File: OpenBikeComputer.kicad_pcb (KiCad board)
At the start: 4 copper layers, 80 x 80 mm, 53 parts, among them J1 USB_C_Receptacle_USB2.0_14P, J2 RJ45_Shielded, J4 Micro_SD_Card_Det1, J5 Conn_01x24_Socket, J6 Conn_01x03_Pin, J7 RFShield_TwoPieces, J8 Conn_01x02_Socket, U1 nRF54L15-QFXX, U2 nPM1300-QEXX, U3 BQ298012RUGR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

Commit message: route SWD lines
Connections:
- J6 pad 1: Net-(J6-Pin_1) -> GND
- J6 pad 3: GND -> Net-(J6-Pin_3)
- U1 pad 25: Net-(J6-Pin_2) -> Net-(J6-Pin_3)
- U1 pad 26: Net-(J6-Pin_1) -> Net-(J6-Pin_2)
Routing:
- net Net-(J6-Pin_2): track 0.00 -> 49.3 mm, vias 0 -> 1
- net Net-(J6-Pin_3): track 0.00 -> 48.8 mm, vias 0 -> 1

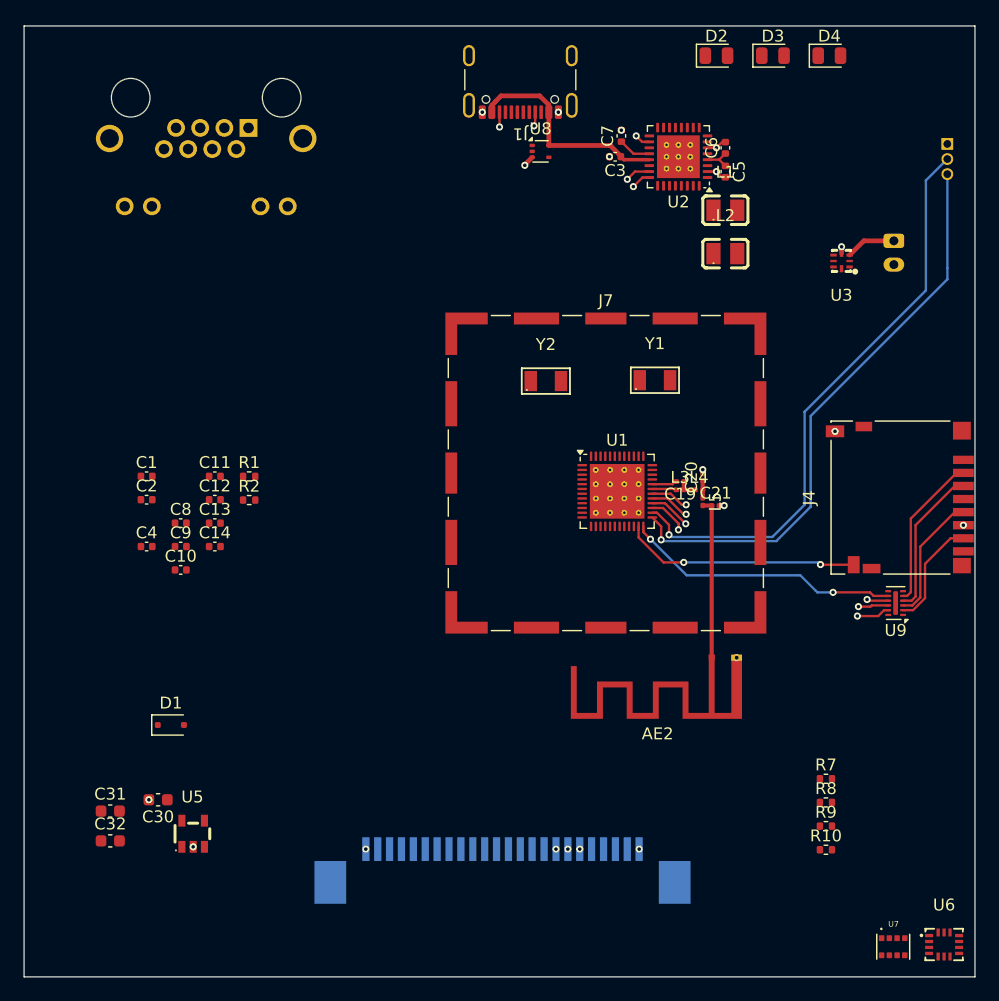
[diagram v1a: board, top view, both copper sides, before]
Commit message: add copper pour on all layers
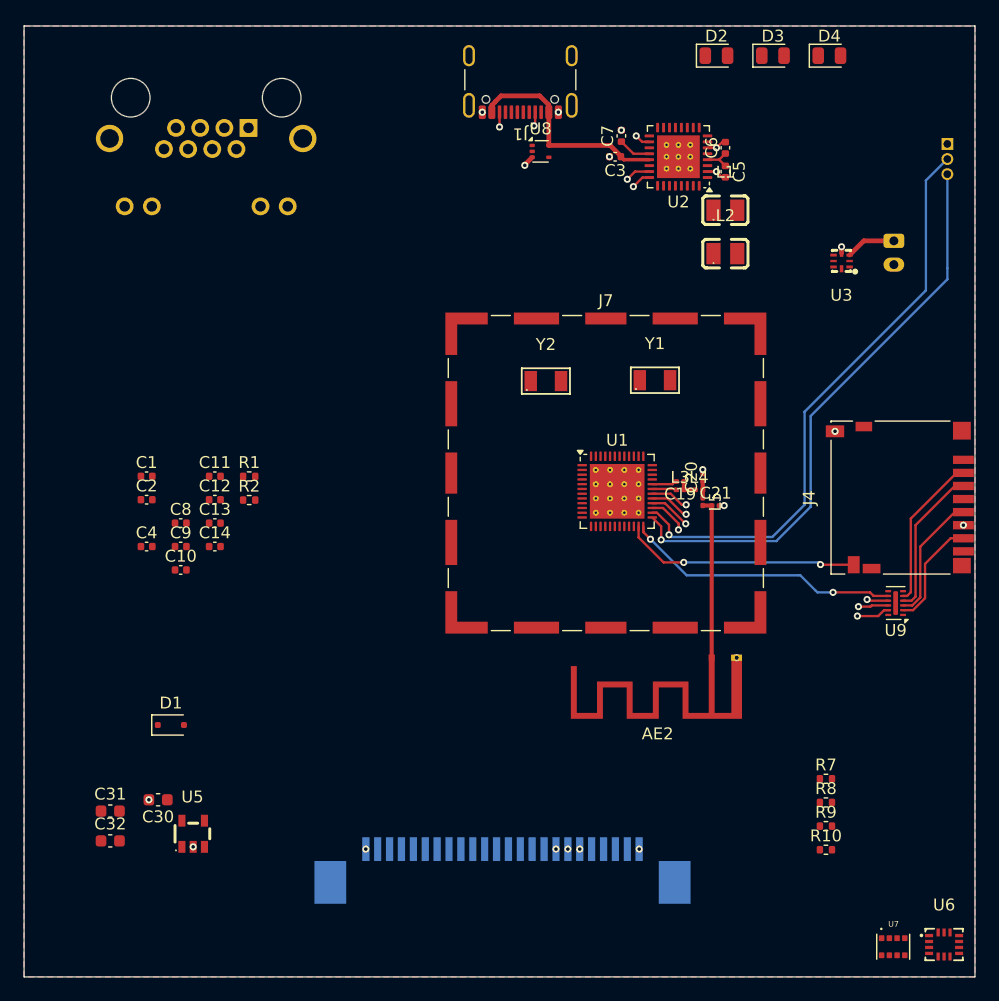
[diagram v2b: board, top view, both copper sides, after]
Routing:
- added copper zone on B.Cu, net GND
- added copper zone on F.Cu, net GND
- added copper zone on In2.Cu, net GND
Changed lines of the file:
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@@
 		(tags "capacitor")
 		(property "Reference" "C30"
-			(at 0 -1.43 360)
+			(at 0 -1.43 0)
 			(layer "F.SilkS")
 			(effects
@@
 		)
 		(property "Value" "4.7uF"
-			(at 0 1.43 360)
+			(at 0 1.43 0)
 			(layer "F.Fab")
 			(effects
@@
 		)
 		(fp_text user "${REFERENCE}"
-			(at 0 0 360)
+			(at 0 0 0)
 			(layer "F.Fab")
 			(effects
@@
 		(tags "capacitor")
 		(property "Reference" "C19"
-			(at 0 -1.05 360)
+			(at 0 -1.05 0)
 			(layer "F.SilkS")
 			(effects
@@
 		)
 		(property "Value" "1.5pF"
-			(at 0 1.05 360)
+			(at 0 1.05 0)
 			(layer "F.Fab")
 			(effects
@@
 		)
 		(fp_text user "${REFERENCE}"
-			(at 0 -0.68 360)
+			(at 0 -0.68 0)
 			(layer "F.Fab")
 			(effects
@@
 		(tags "X2QFN-8_L1.5-W1.5-P0.50-TL footprint C2873374")
 		(property "Reference" "U3"
-			(at 0.012649 -2.877496 360)
+			(at 0.012649 -2.877496 0)
 			(layer "F.SilkS")
 			(effects
@@
 		)
 		(property "Value" "BQ298012RUGR"
-			(at 0.225121 2.800127 360)
+			(at 0.225121 2.800127 0)
 			(layer "F.Fab")
 			(effects
@@
 		)
 		(property "Footprint" "Library:X2QFN-8_L1.5-W1.5-P0.50-TL"
-			(at 0 0 360)
+			(at 0 0 0)
 			(layer "F.Fab")
 			(hide yes)
@@
 		)
 		(property "Datasheet" "https://www.ti.com/cn/lit/ds/symlink/ads7057.pdf?ts=1644852635778"
-			(at 0 0 360)
+			(at 0 0 0)
 			(layer "F.Fab")
 			(hide yes)
@@
 		)
 		(property "Description" ""
-			(at 0 0 360)
+			(at 0 0 0)
 			(layer "F.Fab")
 			(hide yes)
@@
 		)
 		(fp_text user "REF**"
-			(at 53.200121 -26.059873 360)
+			(at 53.200121 -26.059873 0)
 			(layer "F.Fab")
 			(effects
@@
 	)
 	(zone
+		(net 75)
+		(net_name "GND")
+		(layer "F.Cu")
+		(name "$teardrop_padvia$")
+		(hatch full 0.1)
+		(priority 30000)
+		(attr
+			(teardrop
+				(type padvia)
+			)
+		)
+		(connect_pads yes
+			(clearance 0)
+		)
+		(min_thickness 0.0254)
+		(filled_areas_thickness no)
+		(fill yes
+			(thermal_gap 0.5)
+			(thermal_bridge_width 0.5)
+			(island_removal_mode 1)
+			(island_area_min 10)
+		)
+		(polygon
+			(pts
+				(xy 192.661447 86.421396) (xy 192.378604 86.138553) (xy 191.913603 86.512133) (xy 192.125028 86.724972)
+				(xy 192.402899 86.83907)
+			)
+		)
+	)
+	(zone
 		(net 0)
 		(net_name "")
@@
 	)
 	(zone
-		(net 75)
-		(net_name "GND")
-		(layer "F.Cu")
-		(name "$teardrop_padvia$")
-		(hatch full 0.1)
-		(priority 30000)
-		(attr
-			(teardrop
-				(type padvia)
-			)
-		)
-		(connect_pads yes
-			(clearance 0)
-		)
-		(min_thickness 0.0254)
-		(filled_areas_thickness no)
-		(fill yes
-			(thermal_gap 0.5)
-			(thermal_bridge_width 0.5)
-			(island_removal_mode 1)
-			(island_area_min 10)
-		)
-		(polygon
-			(pts
-				(xy 192.661447 86.421396) (xy 192.378604 86.138553) (xy 191.913603 86.512133) (xy 192.125028 86.724972)
-				(xy 192.402899 86.83907)
-			)
-		)
-	)
-	(zone
 		(net 0)
 		(net_name "")
@@
 			)
 		)
+	)
+	(zone
+		(net 75)
+		(net_name "GND")
+		(layers "F.Cu" "In2.Cu" "B.Cu")
+		(hatch edge 0.5)
+		(priority 1)
+		(connect_pads
+			(clearance 0)
+		)
+		(min_thickness 0.25)
+		(filled_areas_thickness no)
+		(fill yes
+			(thermal_gap 0.5)
+			(thermal_bridge_width 0.5)
+		)
+		(polygon
+			(pts
+				(xy 150 75) (xy 230 75) (xy 230 155) (xy 150 155)
+			)
+		)

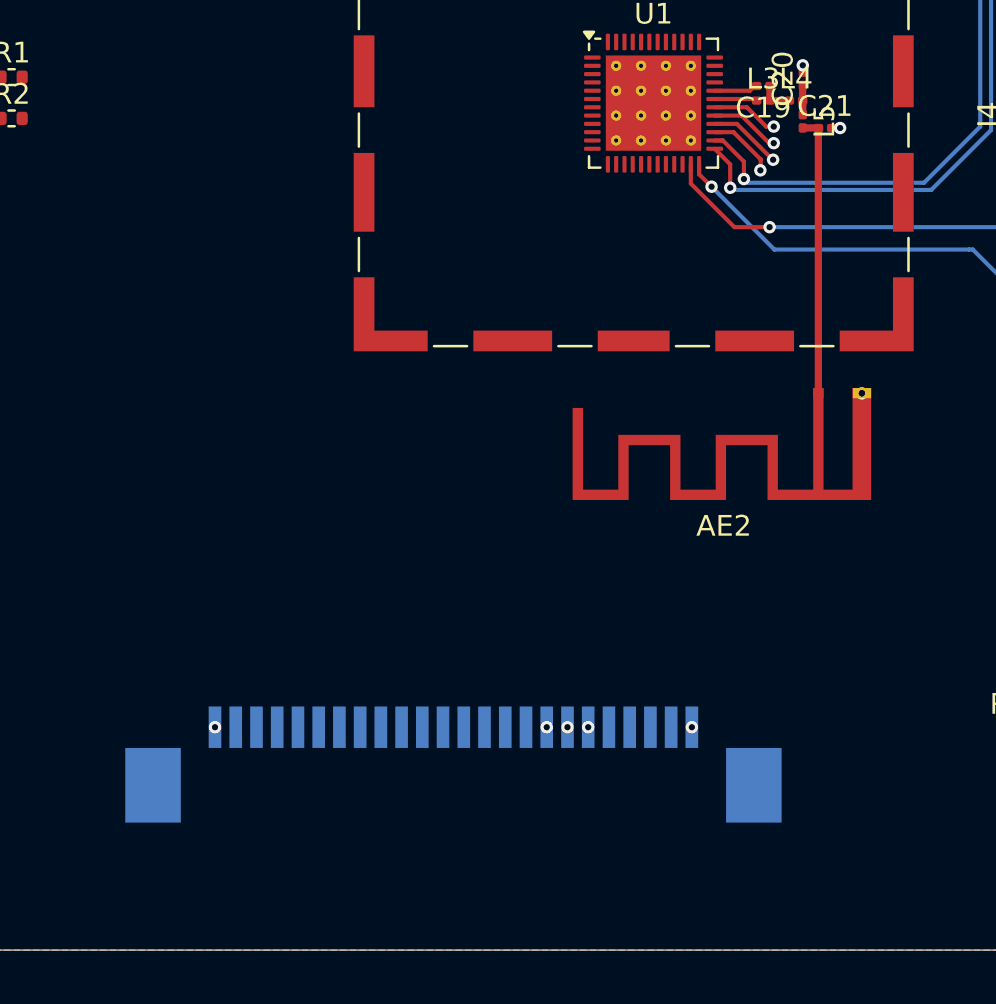
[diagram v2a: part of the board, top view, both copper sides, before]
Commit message: move BT antenna, cleanup keepout zones and transmission line
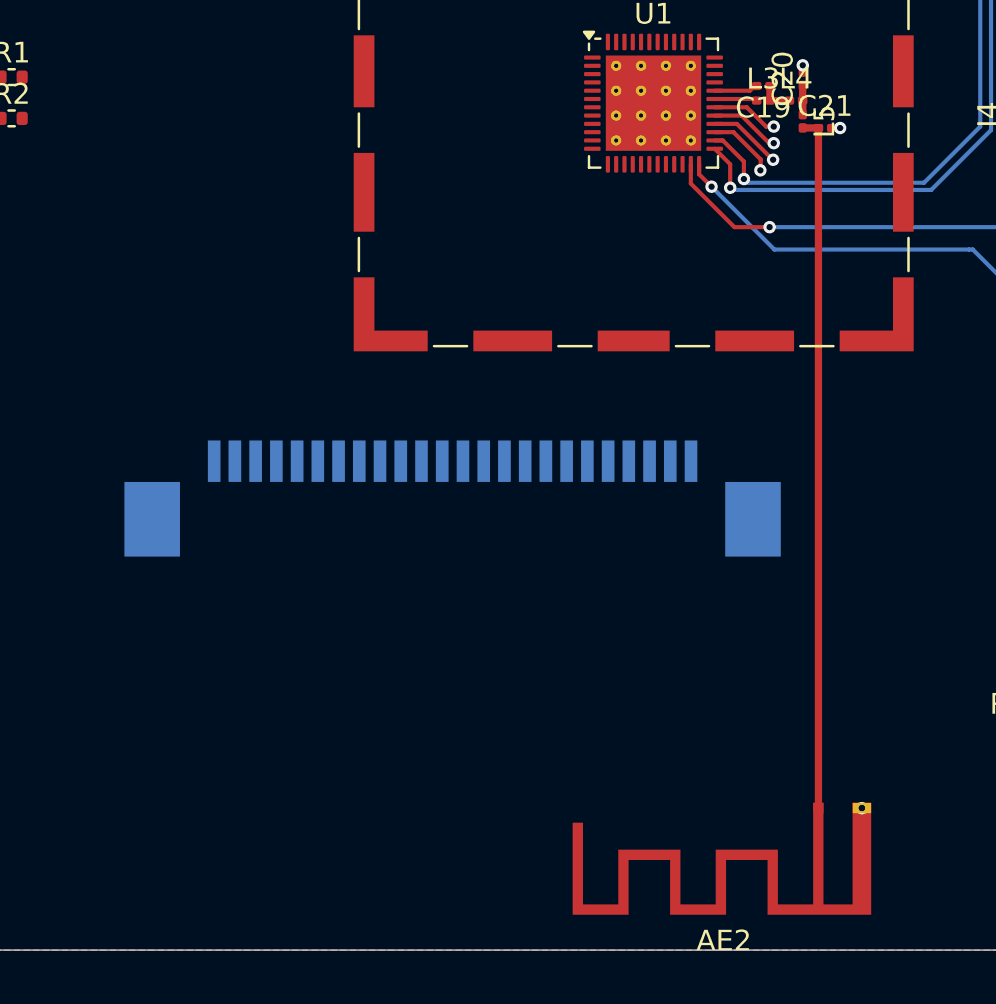
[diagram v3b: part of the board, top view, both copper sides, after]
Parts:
- moved AE2 20.0 mm to (207.8, 148.1)
- moved J5 12.8 mm to (190.2, 133.2)
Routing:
- net Net-(AE2-A): track 13.5 -> 33.7 mm
- net GND: vias 20 -> 15
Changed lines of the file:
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@@
 	(footprint "RF_Antenna:Texas_SWRA117D_2.4GHz_Right"
 		(layer "F.Cu")
-		(at 207.85 128.14 180)
+		(at 207.85 148.145 180)
 		(descr "http://www.ti.com/lit/an/swra117d/swra117d.pdf")
 		(tags "PCB antenna")
@@
 			(pinfunction "Shield")
 			(pintype "passive")
+			(zone_connect 2)
 		)
 		(pad "1" smd rect
@@
 			(pinfunction "Shield")
 			(pintype "passive")
+			(zone_connect 2)
 		)
 		(pad "1" smd rect
@@
 	(footprint "Connector_FFC-FPC:TE_2-84952-4_1x24-1MP_P1.0mm_Horizontal"
 		(layer "B.Cu")
-		(at 190.25 146.05 180)
+		(at 190.21 133.22 180)
 		(descr "TE FPC connector, 24 bottom-side contacts, 1.0mm pitch, 1.0mm height, SMT, http://www.te.com/commerce/DocumentDelivery/DDEController?Action=srchrtrv&DocNm=84952&DocType=Customer+Drawing&DocLang=English&DocFormat=pdf&PartCntxt=84952-4")
 		(tags "te fpc 84952")
@@
 	)
 	(via
-		(at 195.75 144.25)
-		(size 0.6)
-		(drill 0.3)
-		(layers "F.Cu" "B.Cu")
-		(net 75)
-	)
-	(via
 		(at 208.899901 115.349873)
 		(size 0.6)
@@
 	)
 	(via
-		(at 178.75 144.25)
-		(size 0.6)
-		(drill 0.3)
-		(layers "F.Cu" "B.Cu")
-		(net 75)
-	)
-	(via
 		(at 229.025 117)
 		(size 0.6)
@@
 	)
 	(via
-		(at 201.75 144.25)
-		(size 0.6)
-		(drill 0.3)
-		(layers "F.Cu" "B.Cu")
-		(net 75)
-	)
-	(via
-		(at 209.94993 128.15)
+		(at 209.94993 148.155)
 		(size 0.6)
 		(drill 0.3)
@@
 	)
 	(via
-		(at 194.75 144.25)
-		(size 0.6)
-		(drill 0.3)
-		(layers "F.Cu" "B.Cu")
-		(net 75)
-	)
-	(via
 		(at 200.25 83.77)
 		(size 0.6)
@@
 	)
 	(via
-		(at 196.75 144.25)
-		(size 0.6)
-		(drill 0.3)
-		(layers "F.Cu" "B.Cu")
-		(net 75)
-	)
-	(via
 		(at 164.224962 144.060152)
 		(size 0.6)
@@
 	)
 	(segment
-		(start 207.85 115.479802)
-		(end 207.85 128.14)
+		(start 207.099901 115.344873)
+		(end 207.849901 115.344873)
 		(width 0.35)
 		(layer "F.Cu")
@@
 	)
 	(segment
-		(start 207.099901 115.344873)
-		(end 207.849901 115.344873)
+		(start 207.854901 115.474901)
+		(end 207.85 115.479802)
 		(width 0.35)
 		(layer "F.Cu")
@@
 	)
 	(segment
-		(start 207.854901 115.474901)
-		(end 207.85 115.479802)
+		(start 207.854901 148.140099)
+		(end 207.85 148.145)
+		(width 0.35)
+		(layer "F.Cu")
+		(net 105)
+	)
+	(segment
+		(start 207.854901 115.349873)
+		(end 207.854901 148.140099)
 		(width 0.35)
 		(layer "F.Cu")
@@
 	)
 	(zone
-		(net 75)
-		(net_name "GND")
-		(layer "F.Cu")
-		(name "$teardrop_padvia$")
-		(hatch full 0.1)
-		(priority 30000)
-		(attr
-			(teardrop
-				(type padvia)
-			)
-		)
-		(connect_pads yes
-			(clearance 0)
-		)
-		(min_thickness 0.0254)
-		(filled_areas_thickness no)
-		(fill yes
-			(thermal_gap 0.5)
-			(thermal_bridge_width 0.5)
-			(island_removal_mode 1)
-			(island_area_min 10)
-		)
-		(polygon
-			(pts
-				(xy 192.661447 86.421396) (xy 192.378604 86.138553) (xy 191.913603 86.512133) (xy 192.125028 86.724972)
-				(xy 192.402899 86.83907)
-			)
-		)
-	)
-	(zone
-		(net 0)
-		(net_name "")
-		(layer "F.Cu")
-		(hatch edge 0.5)
-		(connect_pads
-			(clearance 0)
-		)
-		(min_thickness 0.25)
-		(filled_areas_thickness no)
-		(keepout
-			(tracks allowed)
-			(vias allowed)
-			(pads not_allowed)
-			(copperpour not_allowed)
-			(footprints allowed)
-		)
-		(fill
-			(thermal_gap 0.5)
-			(thermal_bridge_width 0.5)
-		)
-		(polygon
-			(pts
-				(xy 207.175 115.479802) (xy 207.184207 115.368701) (xy 207.211574 115.26063) (xy 207.256356 115.158538)
-				(xy 207.317331 115.065209) (xy 207.392835 114.983189) (xy 207.48081 114.914715) (xy 207.578856 114.861656)
-				(xy 207.684298 114.825457) (xy 207.794259 114.807108) (xy 207.905741 114.807108) (xy 208.015702 114.825457)
-				(xy 208.121144 114.861656) (xy 208.21919 114.914715) (xy 208.307165 114.983189) (xy 208.382669 115.065209)
-				(xy 208.443644 115.158538) (xy 208.488426 115.26063) (xy 208.515793 115.368701) (xy 208.525 115.479802)
-				(xy 208.525 128.14) (xy 208.515793 128.251101) (xy 208.488426 128.359172) (xy 208.443644 128.461264)
-				(xy 208.382669 128.554593) (xy 208.307165 128.636613) (xy 208.21919 128.705087) (xy 208.121144 128.758146)
-				(xy 208.015702 128.794345) (xy 207.905741 128.812694) (xy 207.794259 128.812694) (xy 207.684298 128.794345)
-				(xy 207.578856 128.758146) (xy 207.48081 128.705087) (xy 207.392835 128.636613) (xy 207.317331 128.554593)
-				(xy 207.256356 128.461264) (xy 207.211574 128.359172) (xy 207.184207 128.251101) (xy 207.175 128.14)
-			)
-		)
-	)
-	(zone
 		(net 0)
 		(net_name "")
@@
 		(net_name "")
 		(layer "F.Cu")
+		(name "antenna")
 		(hatch edge 0.5)
 		(connect_pads
@@
 			(pads not_allowed)
 			(copperpour not_allowed)
-			(footprints allowed)
+			(footprints not_allowed)
 		)
 		(fill
@@
 		(polygon
 			(pts
-				(xy 207.425 115.479802) (xy 207.430797 115.40985) (xy 207.448028 115.341805) (xy 207.476224 115.277525)
-				(xy 207.514616 115.218762) (xy 207.562156 115.16712) (xy 207.617548 115.124007) (xy 207.67928 115.090599)
-				(xy 207.745669 115.067807) (xy 207.814904 115.056254) (xy 207.885096 115.056254) (xy 207.954331 115.067807)
-				(xy 208.02072 115.090599) (xy 208.082452 115.124007) (xy 208.137844 115.16712) (xy 208.185384 115.218762)
-				(xy 208.223776 115.277525) (xy 208.251972 115.341805) (xy 208.269203 115.40985) (xy 208.275 115.479802)
-				(xy 208.275 128.14) (xy 208.269203 128.209952) (xy 208.251972 128.277997) (xy 208.223776 128.342277)
-				(xy 208.185384 128.40104) (xy 208.137844 128.452682) (xy 208.082452 128.495795) (xy 208.02072 128.529203)
-				(xy 207.954331 128.551995) (xy 207.885096 128.563548) (xy 207.814904 128.563548) (xy 207.745669 128.551995)
-				(xy 207.67928 128.529203) (xy 207.617548 128.495795) (xy 207.562156 128.452682) (xy 207.514616 128.40104)
-				(xy 207.476224 128.342277) (xy 207.448028 128.277997) (xy 207.430797 128.209952) (xy 207.425 128.14)
+				(xy 207.429901 115.349873) (xy 207.435698 115.279921) (xy 207.452929 115.211876) (xy 207.481125 115.147596)
+				(xy 207.519517 115.088833) (xy 207.567057 115.037191) (xy 207.622449 114.994078) (xy 207.684181 114.96067)
+				(xy 207.75057 114.937878) (xy 207.819805 114.926325) (xy 207.889997 114.926325) (xy 207.959232 114.937878)
+				(xy 208.025621 114.96067) (xy 208.087353 114.994078) (xy 208.142745 115.037191) (xy 208.190285 115.088833)
+				(xy 208.228677 115.147596) (xy 208.256873 115.211876) (xy 208.274104 115.279921) (xy 208.279901 115.349873)
+				(xy 208.279901 148.140099) (xy 208.274104 148.210051) (xy 208.256873 148.278096) (xy 208.228677 148.342376)
+				(xy 208.190285 148.401139) (xy 208.142745 148.452781) (xy 208.087353 148.495894) (xy 208.025621 148.529302)
+				(xy 207.959232 148.552094) (xy 207.889997 148.563647) (xy 207.819805 148.563647) (xy 207.75057 148.552094)
+				(xy 207.684181 148.529302) (xy 207.622449 148.495894) (xy 207.567057 148.452781) (xy 207.519517 148.401139)
+				(xy 207.481125 148.342376) (xy 207.452929 148.278096) (xy 207.435698 148.210051) (xy 207.429901 148.140099)
 			)
 		)
@@
 	)
 	(zone
+		(net 75)
+		(net_name "GND")
+		(layer "F.Cu")
+		(name "$teardrop_padvia$")
+		(hatch full 0.1)
+		(priority 30000)
+		(attr
+			(teardrop
+				(type padvia)
+			)
+		)
+		(connect_pads yes
+			(clearance 0)
+		)
+		(min_thickness 0.0254)
+		(filled_areas_thickness no)
+		(fill yes
+			(thermal_gap 0.5)
+			(thermal_bridge_width 0.5)
+			(island_removal_mode 1)
+			(island_area_min 10)
+		)
+		(polygon
+			(pts
+				(xy 192.661447 86.421396) (xy 192.378604 86.138553) (xy 191.913603 86.512133) (xy 192.125028 86.724972)
+				(xy 192.402899 86.83907)
+			)
+		)
+	)
+	(zone
 		(net 0)
 		(net_name "")
@@
 		(net 0)
 		(net_name "")
-		(layer "F.Cu")
+		(layers "*.Paste" "*.SilkS" "*.Mask" "F.Cu" "In1.Cu" "In2.Cu" "B.Cu")
+		(name "antenna")
 		(hatch edge 0.5)
 		(connect_pads
@@
 		(filled_areas_thickness no)
 		(keepout
-			(tracks allowed)
-			(vias allowed)
+			(tracks not_allowed)
+			(vias not_allowed)
 			(pads not_allowed)
 			(copperpour not_allowed)
-			(footprints allowed)
+			(footprints not_allowed)
 		)
 		(fill
@@
 		(polygon
 			(pts
-				(xy 207.475 115.479802) (xy 207.480115 115.41808) (xy 207.495319 115.35804) (xy 207.520198 115.301322)
-				(xy 207.554073 115.249473) (xy 207.59602 115.203906) (xy 207.644895 115.165865) (xy 207.699365 115.136388)
-				(xy 207.757943 115.116277) (xy 207.819033 115.106083) (xy 207.880967 115.106083) (xy 207.942057 115.116277)
-				(xy 208.000635 115.136388) (xy 208.055105 115.165865) (xy 208.10398 115.203906) (xy 208.145927 115.249473)
-				(xy 208.179802 115.301322) (xy 208.204681 115.35804) (xy 208.219885 115.41808) (xy 208.225 115.479802)
-				(xy 208.225 128.14) (xy 208.219885 128.201722) (xy 208.204681 128.261762) (xy 208.179802 128.31848)
-				(xy 208.145927 128.370329) (xy 208.10398 128.415896) (xy 208.055105 128.453937) (xy 208.000635 128.483414)
-				(xy 207.942057 128.503525) (xy 207.880967 128.513719) (xy 207.819033 128.513719) (xy 207.757943 128.503525)
-				(xy 207.699365 128.483414) (xy 207.644895 128.453937) (xy 207.59602 128.415896) (xy 207.554073 128.370329)
-				(xy 207.520198 128.31848) (xy 207.495319 128.261762) (xy 207.480115 128.201722) (xy 207.475 128.14)
+				(xy 192.5 155) (xy 214 155.025) (xy 214 147.5) (xy 206.25 147.5) (xy 206.25 144) (xy 192.5 144)
 			)
 		)
@@
 			)
 		)
-	)
-	(zone
-		(net 0)
-		(net_name "")
-		(layers "*.Paste" "*.SilkS" "*.Mask" "In1.Cu" "In2.Cu" "B.Cu")
-		(name "antenna")
-		(hatch edge 0.5)
-		(connect_pads
-			(clearance 0)
-		)
-		(min_thickness 0.25)
-		(filled_areas_thickness no)
-		(keepout
-			(tracks not_allowed)
-			(vias not_allowed)
-			(pads not_allowed)
-			(copperpour not_allowed)
-			(footprints not_allowed)
-		)
-		(fill
-			(thermal_gap 0.5)
-			(thermal_bridge_width 0.5)
-		)
-		(polygon
-			(pts
-				(xy 194.85493 134.28) (xy 211.60493 134.28) (xy 211.60493 128.53) (xy 194.85493 128.53)
-			)
-		)
